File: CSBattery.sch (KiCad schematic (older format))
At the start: 30 parts

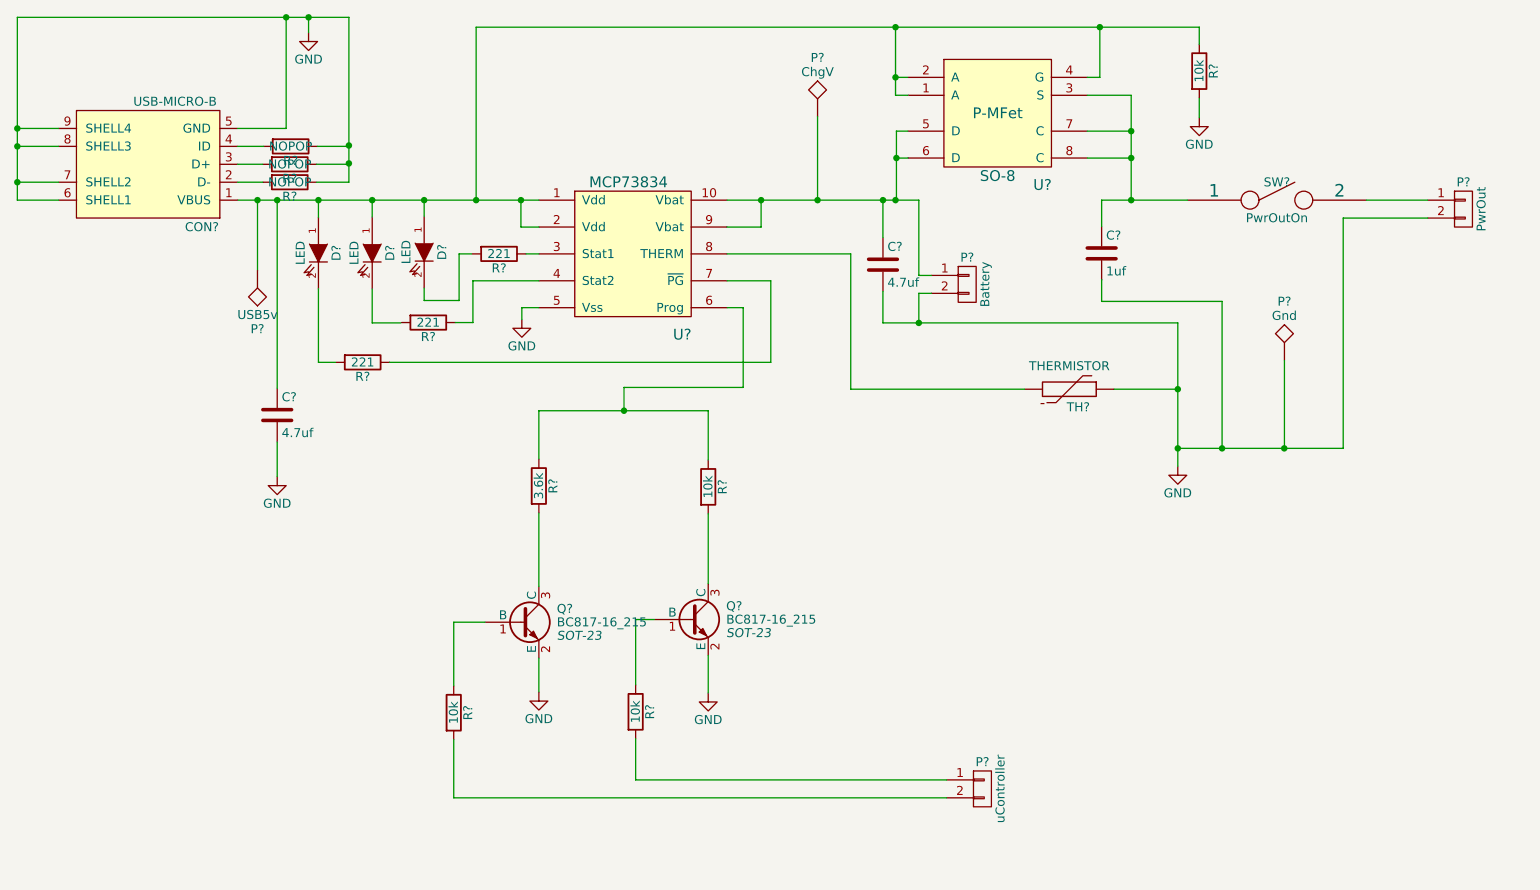
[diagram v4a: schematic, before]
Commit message: assigned footprints, created custom USB footprint and library
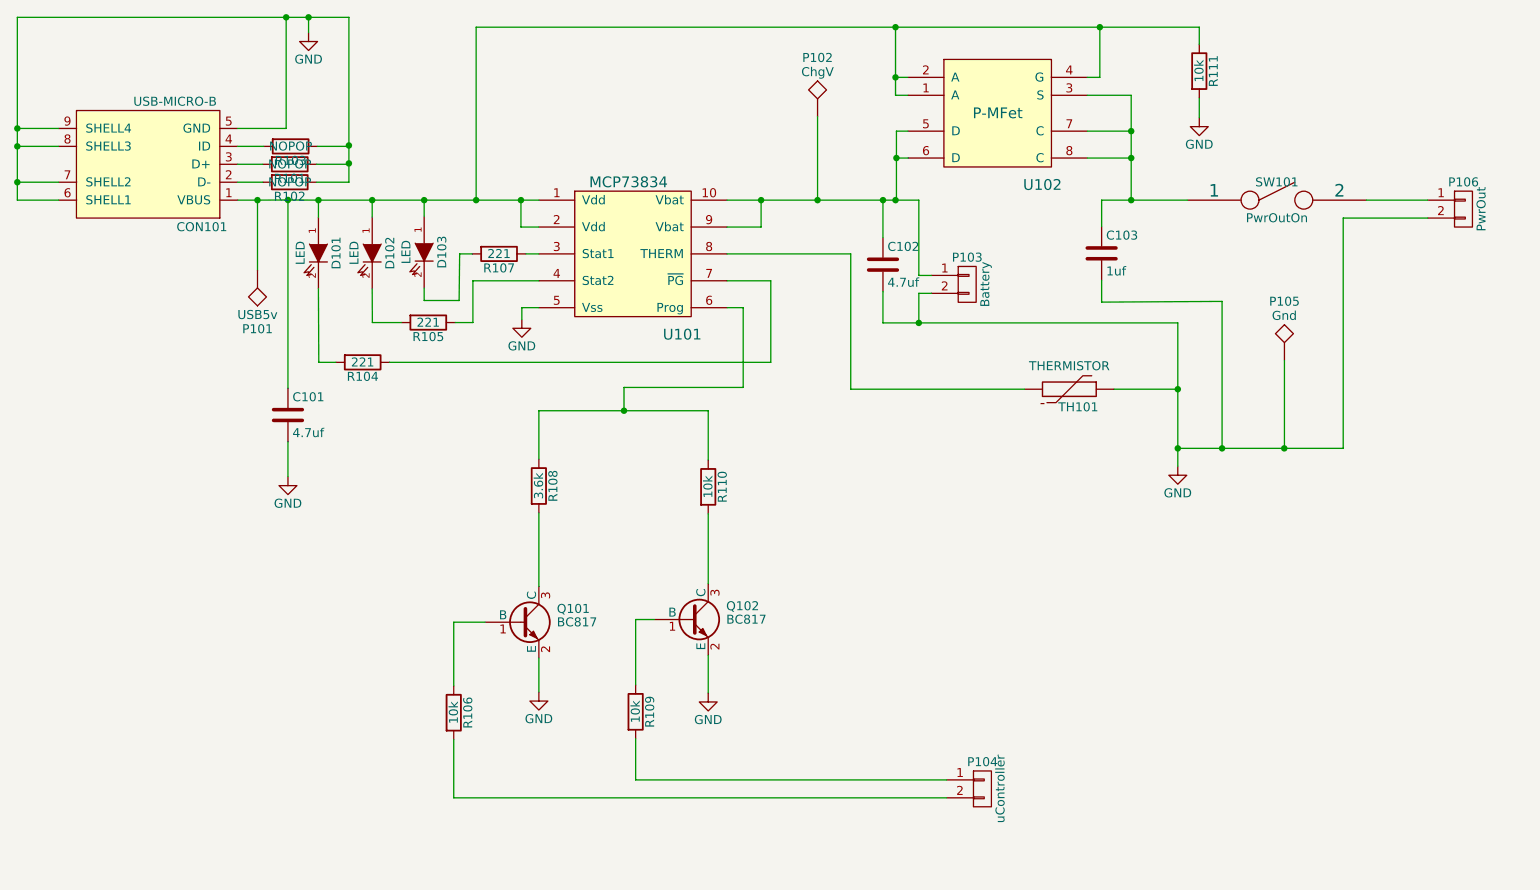
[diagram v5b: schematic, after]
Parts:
- C101, C102: renamed from C?; footprint (none) -> Capacitors_SMD:C_0805_HandSoldering
- C103: renamed from C?; footprint (none) -> Capacitors_SMD:C_0805_HandSoldering; MPN Value -> (none)
- CON101: renamed from CON?; footprint (none) -> CSBattery:USB_Micro-B_Custom; MPN (none) -> 10103594-0001LF
- D101: renamed from D?; footprint (none) -> LEDs:LED-0805; MPN (none) -> KPHCM-2012EC-T
- D102: renamed from D?; footprint (none) -> LEDs:LED-0805; MPN (none) -> 5988160107F
- D103: renamed from D?; footprint (none) -> LEDs:LED-0805; MPN (none) -> OVS-0803
- P101, P102, P105: renamed from P?; footprint (none) -> Measurement_Points:Measurement_Point_Round-TH_Small
- P103, P104, P106: renamed from P?; footprint (none) -> Pin_Headers:Pin_Header_Straight_1x02
- Q101, Q102: renamed from Q?; value BC817-16_215 -> BC817; footprint SOT-23 -> Housings_SOT-23_SOT-143_TSOT-6:SOT-23; MPN Value -> BC817-16_215
- R101, R102, R103, R104, R105, R106, R107, R108, R109, R110, R111: renamed from R?; footprint (none) -> Resistors_SMD:R_0805_HandSoldering
- SW101: renamed from SW?; footprint (none) -> Pin_Headers:Pin_Header_Straight_1x02
- TH101: renamed from TH?; footprint (none) -> Resistors_ThroughHole:Resistor_Horizontal_RM10mm
- U101: renamed from U?; footprint (none) -> Housings_SSOP:MSOP-10_3x3mm_Pitch0.5mm
- U102: renamed from U?; footprint SO-8 -> Power_Integrations:SO-8
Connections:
- wire segments 107 -> 110
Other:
- moved on the sheet: C101

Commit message: amended schematic to incorporate a gnd reference line for the uController signals
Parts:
- removed P104: uController, Pin_Headers:Pin_Header_Straight_1x02, symbol CONN_01X02
- added P104: uController, Pin_Headers:Pin_Header_Straight_1x03, symbol CONN_01X03
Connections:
- net GND: now also P104.3 (P3)
- net at R106.2: now also P104.2 (P2)
- net at R109.2: now also P104.1 (P1)
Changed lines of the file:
@@
-$EndComp
-$Comp
-L CONN_01X02 P104
-U 1 1 55390556
-P 7325 5830
-F 0 "P104" H 7325 5980 50  0000 C CNN
-F 1 "uController" V 7425 5830 50  0000 C CNN
-F 2 "Pin_Headers:Pin_Header_Straight_1x02" H 7325 5830 60  0001 C CNN
-F 3 "" H 7325 5830 60  0000 C CNN
-	1    7325 5830
-	1    0    0    -1
 $EndComp
 $Comp
@@
 Wire Wire Line
 	3921 3228 4083 3228
+$Comp
+L CONN_01X03 P104
+U 1 1 553CB7A6
+P 7325 5880
+F 0 "P104" H 7325 6080 50  0000 C CNN
+F 1 "uController" V 7425 5880 50  0000 C CNN
+F 2 "Pin_Headers:Pin_Header_Straight_1x03" H 7325 5880 60  0001 C CNN
+F 3 "" H 7325 5880 60  0000 C CNN
+	1    7325 5880
+	1    0    0    -1
+$EndComp
+$Comp
+L GND #PWR08
+U 1 1 553CB9A0
+P 6940 6110
+F 0 "#PWR08" H 6940 5860 50  0001 C CNN
+F 1 "GND" H 6940 5960 50  0000 C CNN
+F 2 "" H 6940 6110 60  0000 C CNN
+F 3 "" H 6940 6110 60  0000 C CNN
+	1    6940 6110
+	1    0    0    -1
+$EndComp
+Wire Wire Line
+	6940 6110 6940 5980
+Wire Wire Line
+	6940 5980 7125 5980
 $EndSCHEMATC

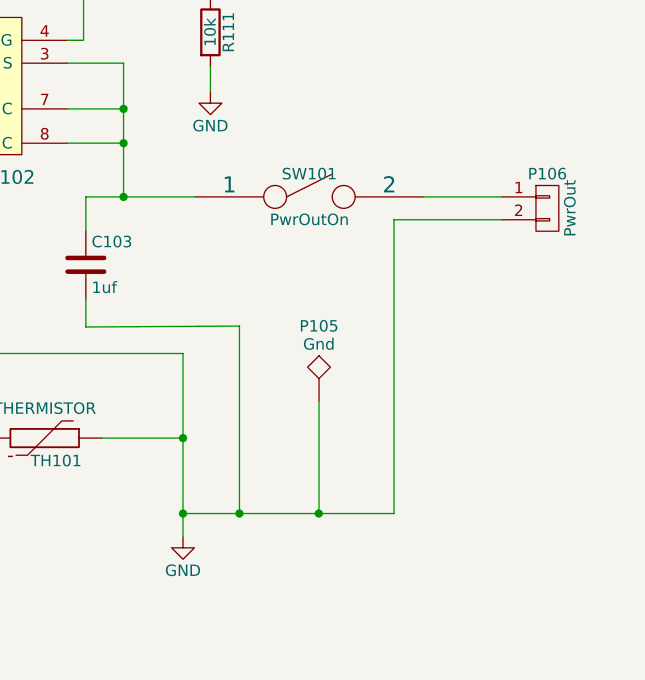
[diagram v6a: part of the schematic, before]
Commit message: updated schematic to include a flyback schottky diode to protect the circuit from Fan inductance
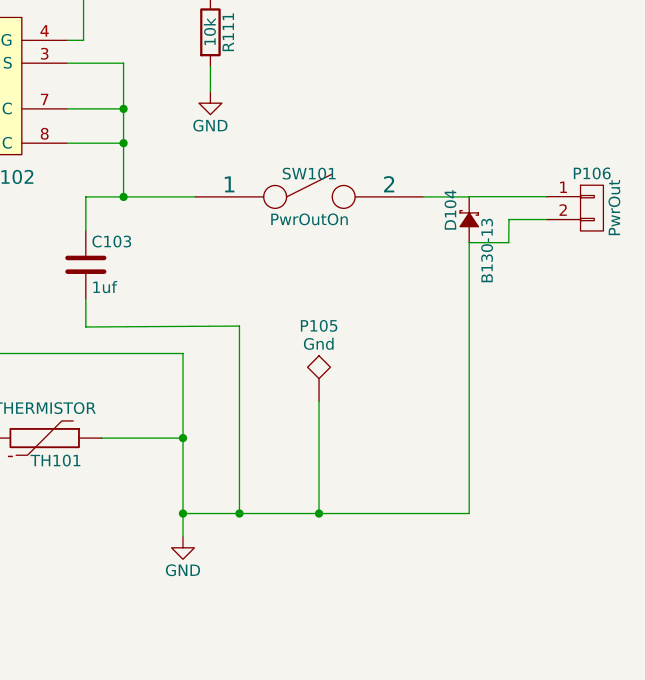
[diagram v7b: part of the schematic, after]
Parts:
- added D104: B130-13, Diodes_SMD:Diode-DO-214BA, symbol D_Schottky_Small
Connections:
- net GND: now also D104.1 (A)
- net at P106.1 (P1), SW101.2: now also D104.2 (C)
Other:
- moved on the sheet: P106
